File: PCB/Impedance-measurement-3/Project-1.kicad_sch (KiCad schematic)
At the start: 68 parts, among them U1 STM32F303CCT6

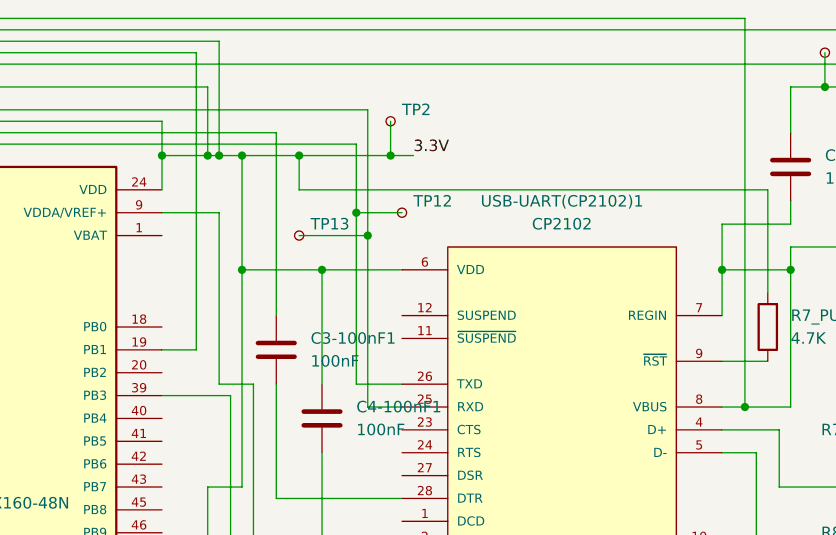
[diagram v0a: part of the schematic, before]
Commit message: mounting holes included 6/7/2026
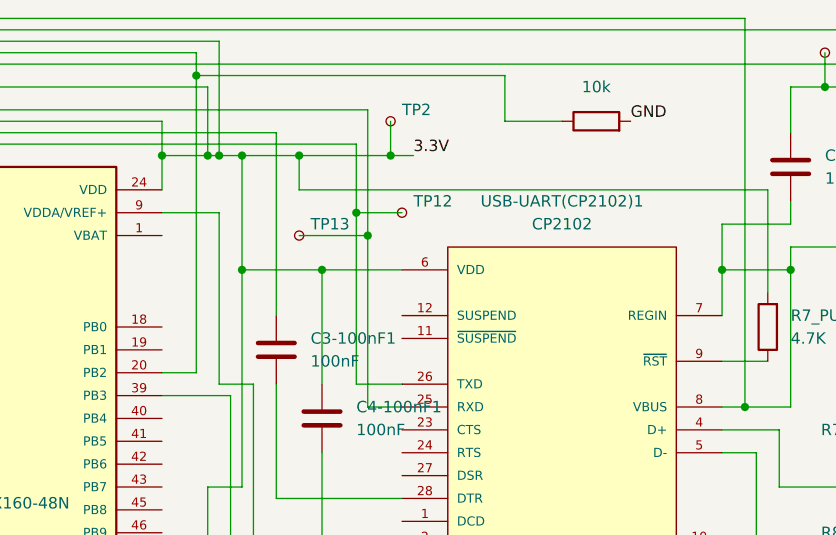
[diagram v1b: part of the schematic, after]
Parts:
- added R25_PULL_10K1: 10k, Resistor_THT:R_Axial_DIN0204_L3.6mm_D1.6mm_P5.08mm_Horizontal, symbol Device:R
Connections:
- net GND: now also R25_PULL_10K1.2
- net at C11-3.3nF1.2, Precision-OP-Amp2.1, R5_1Kohms1.1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: now also U1.20 (PB2), R25_PULL_10K1.1; no longer U1.19 (PB1)
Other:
- title: (none) -> Electrochemical Impedance Spectroscopy
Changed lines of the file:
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@@
 	(generator_version "8.0")
 	(paper "A4")
+	(title_block
+		(title "Electrochemical Impedance Spectroscopy")
+		(date "2026-07-06")
+		(rev "1")
+	)
 	(junction
 		(at 222.25 104.14)
@@
 	)
 	(junction
+		(at 191.77 20.32)
+		(diameter 0)
+		(color 0 0 0 0)
+	)
+	(junction
 		(at 55.88 45.72)
 		(diameter 0)
@@
 	(wire
 		(pts
+			(xy 226.06 20.32) (xy 191.77 20.32)
+		)
+		(stroke
+			(width 0)
+			(type default)
+		)
+	)
+	(wire
+		(pts
+			(xy 191.77 20.32) (xy 191.77 53.34)
+		)
+		(stroke
+			(width 0)
+			(type default)
+		)
+	)
+	(wire
+		(pts
 			(xy 209.55 35.56) (xy 214.63 35.56)
 		)
@@
 	(wire
 		(pts
+			(xy 191.77 17.78) (xy 191.77 20.32)
+		)
+		(stroke
+			(width 0)
+			(type default)
+		)
+	)
+	(wire
+		(pts
 			(xy 120.65 168.91) (xy 151.13 168.91)
 		)
@@
 	(wire
 		(pts
-			(xy 187.96 50.8) (xy 191.77 50.8)
-		)
-		(stroke
-			(width 0)
-			(type default)
-		)
-	)
-	(wire
-		(pts
 			(xy 57.15 60.96) (xy 57.15 58.42)
 		)
@@
 	(wire
 		(pts
+			(xy 226.06 25.4) (xy 226.06 20.32)
+		)
+		(stroke
+			(width 0)
+			(type default)
+		)
+	)
+	(wire
+		(pts
 			(xy 214.63 57.15) (xy 210.82 57.15)
 		)
@@
 	(wire
 		(pts
-			(xy 191.77 50.8) (xy 191.77 17.78)
-		)
-		(stroke
-			(width 0)
-			(type default)
-		)
-	)
-	(wire
-		(pts
 			(xy 213.36 119.38) (xy 213.36 121.92)
 		)
@@
 	(wire
 		(pts
+			(xy 191.77 53.34) (xy 187.96 53.34)
+		)
+		(stroke
+			(width 0)
+			(type default)
+		)
+	)
+	(wire
+		(pts
 			(xy 115.57 48.26) (xy 115.57 93.98)
 		)
@@
 	(wire
 		(pts
+			(xy 232.41 25.4) (xy 226.06 25.4)
+		)
+		(stroke
+			(width 0)
+			(type default)
+		)
+	)
+	(wire
+		(pts
 			(xy 26.67 99.06) (xy 124.46 99.06)
 		)
@@
 		)
 	)
+	(label "GND"
+		(at 240.03 25.4 0)
+		(fields_autoplaced yes)
+		(effects
+			(font
+				(size 1.27 1.27)
+			)
+			(justify left bottom)
+		)
+	)
+	(symbol
+		(lib_id "Device:R")
+		(at 236.22 25.4 90)
+		(unit 1)
+		(exclude_from_sim no)
+		(in_bom yes)
+		(on_board yes)
+		(dnp no)
+		(fields_autoplaced yes)
+		(property "Reference" "R25_PULL_10K1"
+			(at 236.22 19.05 90)
+			(effects
+				(font
+					(size 1.27 1.27)
+				)
+				(hide yes)
+			)
+		)
+		(property "Value" "10k"
+			(at 236.22 21.59 90)
+			(effects
+				(font
+					(size 1.27 1.27)
+				)
+			)
+		)
+		(property "Footprint" "Resistor_THT:R_Axial_DIN0204_L3.6mm_D1.6mm_P5.08mm_Horizontal"
+			(at 236.22 27.178 90)
+			(effects
+				(font
+					(size 1.27 1.27)
+				)
+				(hide yes)
+			)
+		)
+		(property "Datasheet" "~"
+			(at 236.22 25.4 0)
+			(effects
+				(font
+					(size 1.27 1.27)
+				)
+				(hide yes)
+			)
+		)
+		(property "Description" "Resistor"
+			(at 236.22 25.4 0)
+			(effects
+				(font
+					(size 1.27 1.27)
+				)
+				(hide yes)
+			)
+		)
+		(pin "1"
+		)
+		(pin "2"
+		)
+		(instances
+			(project "Project-1"
+				(path "/ded411bd-4c6d-4bca-8aa2-0255249bdd26"
+					(reference "R25_PULL_10K1")
+					(unit 1)
+				)
+			)
+		)
+	)

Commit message: schematic and layout changed 7/7/2026
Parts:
- removed 8MHz-crystal1: ABM3B-8.000MHZ-B2-T, Symbol:XTAL_ABM3B-8.000MHZ-B2-T, symbol 8MHz-crystal:ABM3B-8.000MHZ-B2-T
- removed C7-100nF1: 100nF, Capacitor_THT:C_Axial_L3.8mm_D2.6mm_P7.50mm_Horizontal, symbol Device:C
- removed LDO-Regulator1: MCP1700, Symbol:TO92, symbol LDO-Regulator:MCP1700
- removed Precision-OP-Amp1, Precision-OP-Amp2: OPA2140AID, Symbol:SOIC127P599X175-8N, symbol Precision-OP-Amp:OPA2140AID
- removed SPI-Flash1: W25Q32JVSSIQ, Symbol:SOIC-8_5P28X5P28_WIN, symbol SPI-Flash:W25Q32JVSSIQ
- removed Signal-generator1: AD9833, Symbol:SOP50P490X110-10N, symbol Signal-generator:AD9833
- removed USB-C-power-supply1: USB-C, Symbol:HRO_TYPE-C-31-M-12, symbol USB-C-Power-Supply:USB-C
- removed Voltage-Reference1: ADR4533BRZ, Symbol:R_8_ADI, symbol ADR4533-voltage-reference:ADR4533BRZ
- removed XTAL-25MHz1: ASE-25.000MHZ-LC-T, Symbol:CHIP_ASE-24_ABR, symbol 25MHz-crystal-oscillator2:ASE-25.000MHZ-LC-T
- added 25Mhz-Oscillator1: XO32, Oscillator:Oscillator_SMD_EuroQuartz_XO32-4Pin_3.2x2.5mm, symbol Oscillator:XO32
- added 8MHz-Red-Frequency1: Crystal_GND24, Crystal:Crystal_SMD_5032-4Pin_5.0x3.2mm, symbol Device:Crystal_GND24
- added C11-0.01uF1: 0.01uF, Capacitor_THT:C_Axial_L3.8mm_D2.6mm_P7.50mm_Horizontal, symbol Device:C
- added C3-100nF2: 100nF, Capacitor_THT:C_Axial_L3.8mm_D2.6mm_P7.50mm_Horizontal, symbol Device:C
- added J2: USB_C_Receptacle, Connector_USB:USB_C_Receptacle_GCT_USB4115-03-C, symbol Connector:USB_C_Receptacle
- added Signal-generator2: AD9833BRMZ, Symbol:SOP50P490X110-10N, symbol Signal-Generator-AD9833BRMZ:AD9833BRMZ
- added U2: W25Q32JVSSIQ, Package_SO:SOIC-8_5.23x5.23mm_P1.27mm, symbol SPI-Flash:W25Q32JVSSIQ
- added U5: LM7805_TO220, Package_TO_SOT_THT:TO-220-3_Vertical, symbol Regulator_Linear:LM7805_TO220
- added U9: OPA4141AID, Symbol:SOIC127P600X175-14N, symbol OP-Amp-OPA4141AID:OPA4141AID
- added Voltage-reference1: ISL21080CIH333Z-TK, Symbol:SOT95P237X112-3N, symbol Voltage-Reference-ISL21080CIH333Z-TK:ISL21080CIH333Z-TK
- C10-10uF1: renamed from C10-100nF1; value 100nF -> 10uF
- C12-0.1uF1: renamed from C12-1uF1; value 1uF -> 0.1uF
- C13-10uF1: renamed from C13-100nF1; value 100nF -> 10uF
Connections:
- net Electrode1: now also U9.1 (OUT_A), U9.2 (-IN_A)
- net Electrode2: now also U9.6 (-IN_B)
- net GND: now also R5.1K1.2, 25Mhz-Oscillator1.2 (GND), 8MHz-Red-Frequency1.2, 8MHz-Red-Frequency1.4, C11-0.01uF1.2, C3-100nF2.1, C3-100nF2.2, J2.A1 (GND), J2.A12 (GND), J2.B1 (GND), J2.B12 (GND), J2.S1 (SHIELD), Signal-generator2.4 (DGND), Signal-generator2.9 (AGND), U2.4 (GND), U5.2 (GND), U9.10 (+IN_C), U9.11 (V-), U9.12 (+IN_D), Voltage-reference1.3 (GND); no longer R5.1K1.1
- net VDD: now also 25Mhz-Oscillator1.1 (EN), 25Mhz-Oscillator1.4 (V+), Signal-generator2.2 (VDD), U2.7 (/HOLD_OR_/RESET(IO3)), U2.8 (VCC), U5.3 (VO); no longer C2-100nF1.1
- net at C11-3.3nF1.2, R25_PULL_10K1.1, R5_1Kohms1.1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: now also U9.7 (OUT_B)
- net M-VREF+: now reaches C10-10uF1.1, C14-1uF1.2, R16.1, U1.9 (VDDA/VREF+)
- net M-VREF+: now also C11-0.01uF1.1, Voltage-reference1.2 (VOUT)
- net at C17.2, R15.1, R16.2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: now also U9.5 (+IN_B)
- net at R7-22ohms1.2: now also J2.A6 (D+), J2.B6 (D+)
- net at C13-22pF1.1, U1.6 (PF1/OSC_OUT): now also 8MHz-Red-Frequency1.3
- net at R2_PULL_10K1.1: now also U2.3 (/WP(IO2))
- net at C14-22pF1.1, U1.5 (PF0/OSC_IN): now also 8MHz-Red-Frequency1.1
- net at C1-1nF1.1, R200ohms1.1: now also U9.3 (+IN_A)
- net M-NRST: now reaches C5-100nF1.1, R7_PULL_10K1.1, SWD-connector1.10 (RESET), U1.7 (NRST)
- net M-NRST: now also C3-100nF1.2; no longer C3-100nF1.1
- net at R200ohms1.2, TP4.1: now also Signal-generator2.10 (VOUT)
- net at C15-100nF1.2: now also Signal-generator2.3 (CAP/2.5V)
- net at TP19.1, TP20.1, U1.17 (PA7): now also Signal-generator2.6 (SDATA), U2.5 (DI(IO0))
- net at TP11.1, U1.15 (PA5): now also Signal-generator2.7 (SCLK), U2.6 (CLK)
- net at U1.14 (PA4): now also Signal-generator2.8 (FSYNC)
- net at R5.1K2.2: now also J2.B5 (CC2)
- net M-PA6: now reaches U1.16 (PA6)
- net M-PA6: now also U2.2 (DO(IO1))
- net M-PB13: now reaches R3_PULL_10K1.1, U1.26 (PB13)
- net M-PB13: now also U2.1 (/CS)
- net USB-RXD: now reaches TP13.1, U1.30 (PA9), USB-UART(CP2102)1.25 (RXD)
- net USB-TXD: now reaches TP12.1, U1.31 (PA10), USB-UART(CP2102)1.26 (TXD)
- net at USB-UART(CP2102)1.28 (DTR): now also C3-100nF1.1; no longer C3-100nF1.2
- net at R8-22ohms1.2: now also J2.A7 (D-), J2.B7 (D-)
- net VBUS renamed VBUS-5V
- net VBUS-5V: now also C2-100nF1.1, J2.A4 (VBUS), J2.A9 (VBUS), J2.B4 (VBUS), J2.B9 (VBUS), U5.1 (VI), U9.4 (V+), Voltage-reference1.1 (VIN)
- new net: J2.A5 (CC1), R5.1K1.1
- new net: 25Mhz-Oscillator1.3 (OUT), Signal-generator2.5 (MCLK)
- new net O_C: U9.8 (OUT_C), U9.9 (-IN_C)
- new net O_D: U9.13 (-IN_D), U9.14 (OUT_D)
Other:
- moved on the sheet: C1-1nF1, C13-10uF1, C15-100nF1, C3-100nF1, C6-100nF1, R5.1K1, TP13, TP4, TP5
